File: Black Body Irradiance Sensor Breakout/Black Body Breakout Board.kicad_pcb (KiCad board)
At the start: 2 copper layers, 14 x 9 mm, 6 parts, among them J2 Conn_01x02, U1 TSL25911FN

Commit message: connector update
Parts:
- removed J2: Conn_01x02, Connector_Molex:Molex_Nano-Fit_105313-xx02_1x02_P2.50mm_Horizontal
- added J1: Conn_01x06, Connector_Molex:Molex_Nano-Fit_105313-xx06_1x06_P2.50mm_Horizontal, F.Cu at (123.5, 77.0)
- moved R2 5.06 mm to (125.0, 73.0), turned to -90 degrees
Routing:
- net GND: track 5.04 -> 11.3 mm, vias 0 -> 2
- net Net-(J1-Pin_6): track 6.96 -> 10.6 mm
- net Net-(J1-Pin_4): track 14.9 -> 17.4 mm, vias 2 -> 3
- net Net-(J1-Pin_5): track 9.39 -> 10.0 mm
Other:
- board size 14 x 9 mm -> 18.6 x 14.1 mm

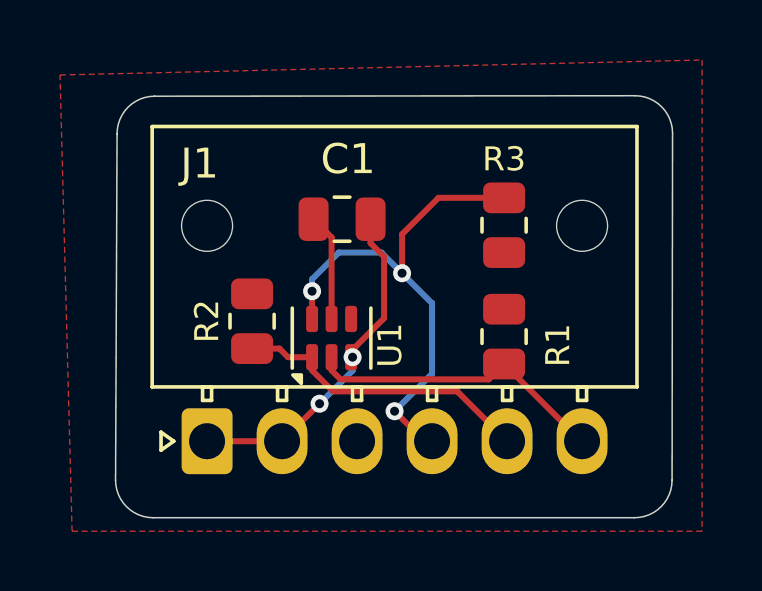
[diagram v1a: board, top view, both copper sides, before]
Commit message: updated connectors
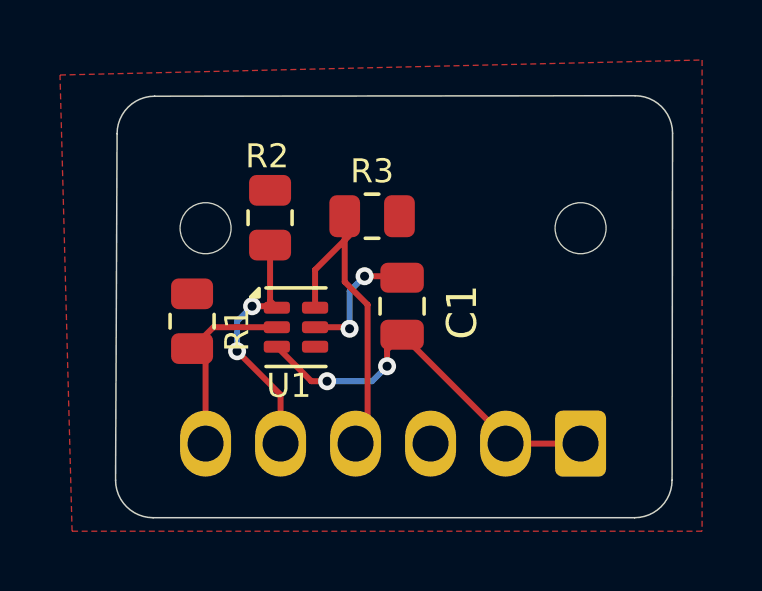
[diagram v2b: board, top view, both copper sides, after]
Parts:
- J1: moved to B.Cu
- moved J1 12.5 mm to (135.9, 77.1)
- moved R1 10.4 mm to (123.0, 73.0)
- moved R3 4.41 mm to (129.0, 69.5), turned to 180 degrees
- moved C1 3.52 mm to (130.0, 72.5), turned to 90 degrees
- moved R2 3.50 mm to (125.6, 69.5)
- moved U1 1.24 mm to (126.5, 73.2), turned to 0 degrees
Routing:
- net Net-(J1-Pin_4): track 17.4 -> 11.8 mm, vias 3 -> 0
- net Net-(J1-Pin_6): track 10.6 -> 6.47 mm
- net GND: track 11.3 -> 13.5 mm
- net Net-(J1-Pin_5): track 10.0 -> 8.41 mm, vias 0 -> 2
- net +3V3: track 3.91 -> 4.40 mm, vias 0 -> 2

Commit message: updated connectors
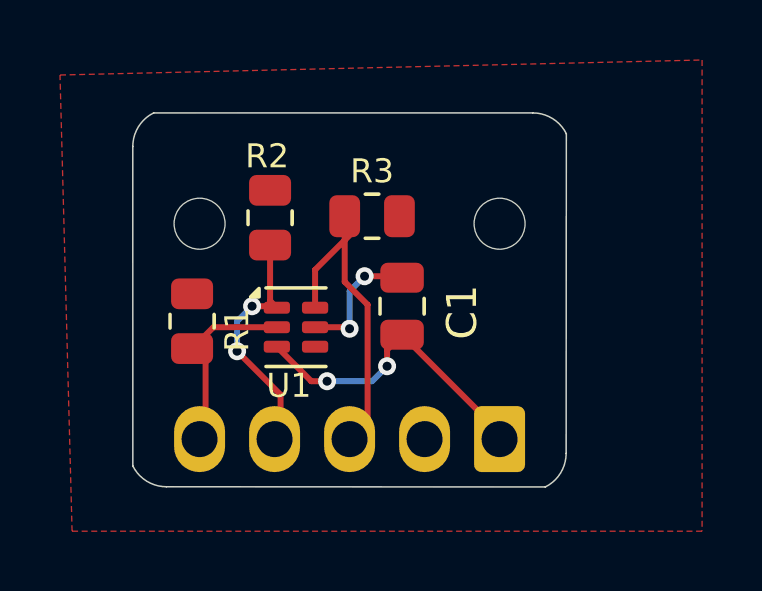
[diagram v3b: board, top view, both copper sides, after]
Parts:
- removed J1: Conn_01x06, Connector_Molex:Molex_Nano-Fit_105313-xx06_1x06_P2.50mm_Horizontal
- added J2: Conn_01x05, Connector_Molex:Molex_Nano-Fit_105313-xx05_1x05_P2.50mm_Horizontal, B.Cu at (133.2, 76.9)
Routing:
- net GND: track 13.5 -> 11.0 mm
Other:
- board size 18.6 x 14.1 mm -> 14.5 x 12.5 mm
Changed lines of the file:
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@@
 	(net 1 "+3V3")
 	(net 2 "GND")
-	(net 3 "Net-(J1-Pin_5)")
+	(net 3 "Net-(J2-Pin_4)")
 	(net 4 "unconnected-(U1-NC-Pad4)")
-	(net 5 "Net-(J1-Pin_6)")
-	(net 6 "Net-(J1-Pin_4)")
+	(net 5 "Net-(J2-Pin_5)")
+	(net 6 "Net-(J2-Pin_3)")
 	(footprint "Resistor_SMD:R_0805_2012Metric"
 		(layer "F.Cu")
@@
 			(layers "F.Cu" "F.Mask" "F.Paste")
 			(roundrect_rratio 0.243902)
-			(net 3 "Net-(J1-Pin_5)")
+			(net 3 "Net-(J2-Pin_4)")
 			(pintype "passive")
 		)
@@
 			(layers "F.Cu" "F.Mask" "F.Paste")
 			(roundrect_rratio 0.243902)
-			(net 5 "Net-(J1-Pin_6)")
+			(net 5 "Net-(J2-Pin_5)")
 			(pintype "passive")
 		)
@@
 			(layers "F.Cu" "F.Mask" "F.Paste")
 			(roundrect_rratio 0.243902)
-			(net 6 "Net-(J1-Pin_4)")
+			(net 6 "Net-(J2-Pin_3)")
 			(pintype "passive")
 		)
@@
 			(layers "F.Cu" "F.Mask" "F.Paste")
 			(roundrect_rratio 0.25)
-			(net 3 "Net-(J1-Pin_5)")
+			(net 3 "Net-(J2-Pin_4)")
 			(pinfunction "SCL")
 			(pintype "input")
@@
 			(layers "F.Cu" "F.Mask" "F.Paste")
 			(roundrect_rratio 0.25)
-			(net 5 "Net-(J1-Pin_6)")
+			(net 5 "Net-(J2-Pin_5)")
 			(pinfunction "INT")
 			(pintype "open_collector")
@@
 			(layers "F.Cu" "F.Mask" "F.Paste")
 			(roundrect_rratio 0.25)
-			(net 6 "Net-(J1-Pin_4)")
+			(net 6 "Net-(J2-Pin_3)")
 			(pinfunction "SDA")
 			(pintype "bidirectional")
@@
 		)
 	)
-	(footprint "Connector_Molex:Molex_Nano-Fit_105313-xx06_1x06_P2.50mm_Horizontal"
+	(footprint "Connector_Molex:Molex_Nano-Fit_105313-xx05_1x05_P2.50mm_Horizontal"
 		(layer "B.Cu")
-		(at 135.95 77.08 90)
-		(descr "Molex Nano-Fit Power Connectors, 105313-xx06, 6 Pins per row (http://www.molex.com/pdm_docs/sd/1053131208_sd.pdf), generated with kicad-footprint-generator")
+		(at 133.25 76.93 90)
+		(descr "Molex Nano-Fit Power Connectors, 105313-xx05, 5 Pins per row (http://www.molex.com/pdm_docs/sd/1053131208_sd.pdf), generated with kicad-footprint-generator")
 		(tags "connector Molex Nano-Fit horizontal")
-		(property "Reference" "J1"
-			(at 9.25 0.25 0)
+		(property "Reference" "J2"
+			(at 6.15 2.92 90)
 			(layer "B.SilkS")
 			(effects
@@
 			)
 		)
-		(property "Value" "Conn_01x06"
-			(at 6.15 -15.42 90)
+		(property "Value" "Conn_01x05"
+			(at 6.15 -12.92 90)
 			(layer "B.Fab")
 			(effects
@@
 			)
 		)
-		(property "Description" "Generic connector, single row, 01x06, script generated (kicad-library-utils/schlib/autogen/connector/)"
+		(property "Description" "Generic connector, single row, 01x05, script generated (kicad-library-utils/schlib/autogen/connector/)"
 			(at 0 0 90)
 			(layer "B.Fab")
@@
 		(attr through_hole)
 		(fp_line
-			(start 10.49 -14.33)
+			(start 10.49 -11.83)
 			(end 10.49 1.83)
 			(stroke
@@
 		)
 		(fp_line
-			(start 1.81 -14.33)
-			(end 10.49 -14.33)
-			(stroke
-				(width 0.12)
-				(type solid)
-			)
-			(layer "B.SilkS")
-		)
-		(fp_line
-			(start 1.81 -12.65)
-			(end 1.81 -12.35)
-			(stroke
-				(width 0.12)
-				(type solid)
-			)
-			(layer "B.SilkS")
-		)
-		(fp_line
-			(start 1.36 -12.65)
-			(end 1.81 -12.65)
-			(stroke
-				(width 0.12)
-				(type solid)
-			)
-			(layer "B.SilkS")
-		)
-		(fp_line
-			(start 1.81 -12.35)
-			(end 1.36 -12.35)
-			(stroke
-				(width 0.12)
-				(type solid)
-			)
-			(layer "B.SilkS")
-		)
-		(fp_line
-			(start 1.36 -12.35)
-			(end 1.36 -12.65)
+			(start 1.81 -11.83)
+			(end 10.49 -11.83)
 			(stroke
 				(width 0.12)
@@
 		(fp_line
 			(start 1.81 1.83)
-			(end 1.81 -14.33)
-			(stroke
-				(width 0.12)
-				(type solid)
-			)
-			(layer "B.SilkS")
-		)
-		(fp_line
-			(start 10.88 -14.72)
+			(end 1.81 -11.83)
+			(stroke
+				(width 0.12)
+				(type solid)
+			)
+			(layer "B.SilkS")
+		)
+		(fp_line
+			(start 10.88 -12.22)
 			(end 10.88 2.22)
 			(stroke
@@
 		)
 		(fp_line
-			(start -1.6 -14.72)
-			(end 10.88 -14.72)
+			(start -1.6 -12.22)
+			(end 10.88 -12.22)
 			(stroke
 				(width 0.05)
@@
 		(fp_line
 			(start -1.6 2.22)
-			(end -1.6 -14.72)
+			(end -1.6 -12.22)
 			(stroke
 				(width 0.05)
@@
 		)
 		(fp_line
-			(start 10.38 -14.22)
+			(start 10.38 -11.72)
 			(end 10.38 1.72)
 			(stroke
@@
 		)
 		(fp_line
-			(start 1.92 -14.22)
-			(end 10.38 -14.22)
+			(start 1.92 -11.72)
+			(end 10.38 -11.72)
 			(stroke
 				(width 0.1)
@@
 		(fp_line
 			(start 1.92 1.72)
-			(end 1.92 -14.22)
+			(end 1.92 -11.72)
 			(stroke
 				(width 0.1)
@@
 		)
 		(fp_text user "${REFERENCE}"
-			(at 6.15 -13.52 90)
+			(at 6.15 -11.02 90)
 			(layer "B.Fab")
 			(effects
@@
 		)
 		(pad "" np_thru_hole circle
-			(at 7.18 -12.5 90)
+			(at 7.18 -10 90)
 			(size 1.7 1.7)
 			(drill 1.7)
@@
 			(layers "*.Cu" "*.Mask")
 			(remove_unused_layers no)
-			(net 2 "GND")
+			(net 1 "+3V3")
 			(pinfunction "Pin_2")
 			(pintype "passive")
@@
 			(layers "*.Cu" "*.Mask")
 			(remove_unused_layers no)
-			(net 1 "+3V3")
+			(net 6 "Net-(J2-Pin_3)")
 			(pinfunction "Pin_3")
 			(pintype "passive")
@@
 			(layers "*.Cu" "*.Mask")
 			(remove_unused_layers no)
-			(net 6 "Net-(J1-Pin_4)")
+			(net 3 "Net-(J2-Pin_4)")
 			(pinfunction "Pin_4")
 			(pintype "passive")
@@
 			(layers "*.Cu" "*.Mask")
 			(remove_unused_layers no)
-			(net 3 "Net-(J1-Pin_5)")
+			(net 5 "Net-(J2-Pin_5)")
 			(pinfunction "Pin_5")
 			(pintype "passive")
 		)
-		(pad "6" thru_hole oval
-			(at 0 -12.5 90)
-			(size 2.2 1.7)
-			(drill 1.2)
-			(layers "*.Cu" "*.Mask")
-			(remove_unused_layers no)
-			(net 5 "Net-(J1-Pin_6)")
-			(pinfunction "Pin_6")
-			(pintype "passive")
-		)
 		(embedded_fonts no)
-		(model "${KICAD9_3DMODEL_DIR}/Connector_Molex.3dshapes/Molex_Nano-Fit_105313-xx06_1x06_P2.50mm_Horizontal.step"
+		(model "${KICAD9_3DMODEL_DIR}/Connector_Molex.3dshapes/Molex_Nano-Fit_105313-xx05_1x05_P2.50mm_Horizontal.step"
 			(offset
 				(xyz 0 0 0)
@@
 	)
 	(gr_line
-		(start 137.7661 65.483883)
-		(end 121.75 65.5)
+		(start 121.025 77.824967)
+		(end 121.023544 67.17694)
 		(stroke
 			(width 0.05)
@@
 	)
 	(gr_arc
-		(start 137.766117 65.483883)
-		(mid 138.65 65.85)
-		(end 139.016117 66.733883)
+		(start 134.355741 66.05656)
+		(mid 135.014072 66.243969)
+		(end 135.475 66.75)
 		(stroke
 			(width 0.05)
@@
 	)
 	(gr_arc
-		(start 120.5 66.75)
-		(mid 120.866117 65.866117)
-		(end 121.75 65.5)
+		(start 122.144259 78.51844)
+		(mid 121.485928 78.331031)
+		(end 121.025 77.825)
 		(stroke
 			(width 0.05)
@@
 		(layer "Edge.Cuts")
 	)
-	(gr_line
-		(start 121.7 79.55)
-		(end 137.75 79.55)
+	(gr_arc
+		(start 135.46844 77.405741)
+		(mid 135.281031 78.064072)
+		(end 134.775 78.525)
 		(stroke
 			(width 0.05)
@@
 	)
 	(gr_arc
-		(start 121.7 79.55)
-		(mid 120.816117 79.183883)
-		(end 120.45 78.3)
+		(start 121.023543 67.17694)
+		(mid 121.210952 66.518609)
+		(end 121.716983 66.057681)
 		(stroke
 			(width 0.05)
@@
 	)
 	(gr_line
-		(start 139.016116 66.733883)
-		(end 139 78.3)
+		(start 121.716983 66.057681)
+		(end 134.3557 66.05656)
 		(stroke
 			(width 0.05)
@@
 	)
 	(gr_line
-		(start 120.5 66.75)
-		(end 120.45 78.3)
+		(start 134.775 78.524983)
+		(end 122.1443 78.51844)
 		(stroke
 			(width 0.05)
@@
 		(layer "Edge.Cuts")
 	)
-	(gr_arc
-		(start 139 78.3)
-		(mid 138.633883 79.183883)
-		(end 137.75 79.55)
+	(gr_line
+		(start 135.475 66.750033)
+		(end 135.468439 77.405741)
 		(stroke
 			(width 0.05)
@@
 		(width 0.2)
 		(layer "F.Cu")
-		(net 2)
-	)
-	(segment
-		(start 135.95 77.08)
-		(end 133.45 77.08)
-		(width 0.2)
-		(layer "F.Cu")

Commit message: fixed edge cuts BO
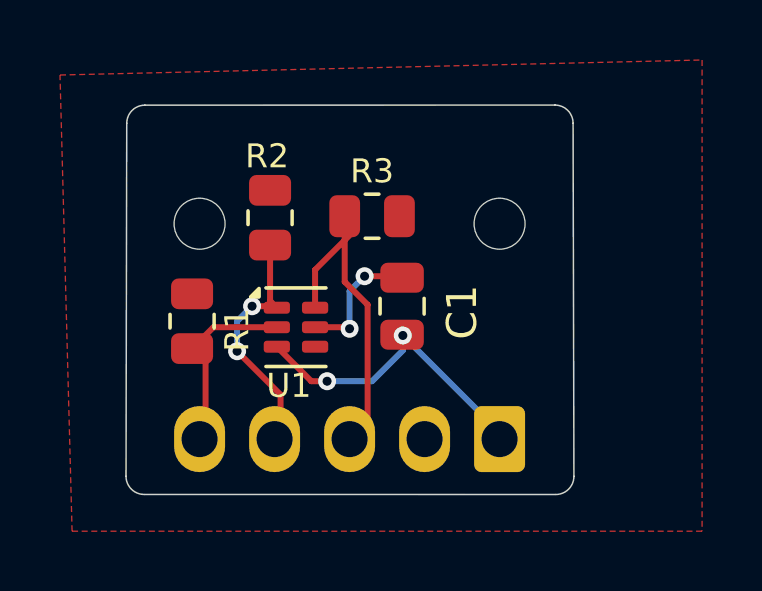
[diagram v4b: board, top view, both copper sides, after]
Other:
- board size 14.5 x 12.5 mm -> 14.9 x 13 mm
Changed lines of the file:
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@@
 		(tags "connector Molex Nano-Fit horizontal")
 		(property "Reference" "J2"
-			(at 6.15 2.92 90)
+			(at 4.955 1.05 90)
 			(layer "B.SilkS")
 			(effects
@@
 		)
 	)
+	(gr_arc
+		(start 120.821673 66.40099)
+		(mid 121 65.975)
+		(end 121.426878 65.798806)
+		(stroke
+			(width 0.05)
+			(type default)
+		)
+		(layer "Edge.Cuts")
+	)
 	(gr_line
-		(start 121.025 77.824967)
-		(end 121.023544 67.17694)
+		(start 120.821674 66.40099)
+		(end 120.797816 78.164524)
 		(stroke
 			(width 0.05)
@@
 	)
 	(gr_arc
-		(start 134.355741 66.05656)
-		(mid 135.014072 66.243969)
-		(end 135.475 66.75)
+		(start 135.097816 65.794795)
+		(mid 135.523806 65.973122)
+		(end 135.7 66.4)
 		(stroke
 			(width 0.05)
@@
 	)
 	(gr_arc
-		(start 122.144259 78.51844)
-		(mid 121.485928 78.331031)
-		(end 121.025 77.825)
+		(start 121.4 78.775)
+		(mid 120.97401 78.596673)
+		(end 120.797816 78.169795)
+		(stroke
+			(width 0.05)
+			(type default)
+		)
+		(layer "Edge.Cuts")
+	)
+	(gr_line
+		(start 135.097816 65.794796)
+		(end 121.426878 65.798806)
+		(stroke
+			(width 0.05)
+			(type default)
+		)
+		(layer "Edge.Cuts")
+	)
+	(gr_line
+		(start 121.40591 78.775)
+		(end 135.116142 78.776194)
 		(stroke
 			(width 0.05)
@@
 	)
 	(gr_arc
-		(start 135.46844 77.405741)
-		(mid 135.281031 78.064072)
-		(end 134.775 78.525)
-		(stroke
-			(width 0.05)
-			(type default)
-		)
-		(layer "Edge.Cuts")
-	)
-	(gr_arc
-		(start 121.023543 67.17694)
-		(mid 121.210952 66.518609)
-		(end 121.716983 66.057681)
+		(start 135.728327 78.17401)
+		(mid 135.55 78.6)
+		(end 135.123122 78.776194)
 		(stroke
 			(width 0.05)
@@
 	)
 	(gr_line
-		(start 121.716983 66.057681)
-		(end 134.3557 66.05656)
-		(stroke
-			(width 0.05)
-			(type default)
-		)
-		(layer "Edge.Cuts")
-	)
-	(gr_line
-		(start 134.775 78.524983)
-		(end 122.1443 78.51844)
-		(stroke
-			(width 0.05)
-			(type default)
-		)
-		(layer "Edge.Cuts")
-	)
-	(gr_line
-		(start 135.475 66.750033)
-		(end 135.468439 77.405741)
+		(start 135.7 66.403811)
+		(end 135.728327 78.17401)
 		(stroke
 			(width 0.05)
@@
 	)
 	(segment
-		(start 130 73.45)
-		(end 133.45 76.9)
-		(width 0.2)
-		(layer "F.Cu")
-		(net 2)
-	)
-	(segment
 		(start 126.975 75)
 		(end 127.5 75)
@@
 	)
 	(segment
-		(start 129.5 73.95)
-		(end 130 73.45)
-		(width 0.2)
-		(layer "F.Cu")
-		(net 2)
-	)
-	(segment
 		(start 133.45 76.9)
 		(end 133.45 77.08)
@@
 		(width 0.2)
 		(layer "F.Cu")
-		(net 2)
-	)
-	(segment
-		(start 129.5 74.5)
-		(end 129.5 73.95)
-		(width 0.2)
-		(layer "F.Cu")
-		(net 2)
-	)
-	(via
-		(at 129.5 74.5)
-		(size 0.6)
-		(drill 0.3)
-		(layers "F.Cu" "B.Cu")
 		(net 2)
 	)
@@
 		(net 2)
 	)
+	(via
+		(at 130.025 73.475)
+		(size 0.6)
+		(drill 0.3)
+		(layers "F.Cu" "B.Cu")
+		(net 2)
+	)
+	(segment
+		(start 133.25 76.93)
+		(end 133.25 76.7)
+		(width 0.2)
+		(layer "B.Cu")
+		(net 2)
+	)
 	(segment
 		(start 129 75)
-		(end 129.5 74.5)
+		(end 130.025 73.975)
 		(width 0.2)
 		(layer "B.Cu")
+		(net 2)
+	)
+	(segment
+		(start 133.25 76.7)
+		(end 130.025 73.475)
+		(width 0.2)
+		(layer "B.Cu")
+		(net 2)
+	)
+	(segment
+		(start 130.025 73.975)
+		(end 130.025 73.475)
+		(width 0.2)
+		(layer "B.Cu")
